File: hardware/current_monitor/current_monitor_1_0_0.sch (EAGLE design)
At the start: 60 parts, among them Q1 RZQ045P01CT, Q2 APDS-9002, U1 PIC18F46J50, U4 MAX4372, U5 TC1046, U6 AT45DB041BWIDE, U7 AT45DB041BWIDE, X1 USBSMD

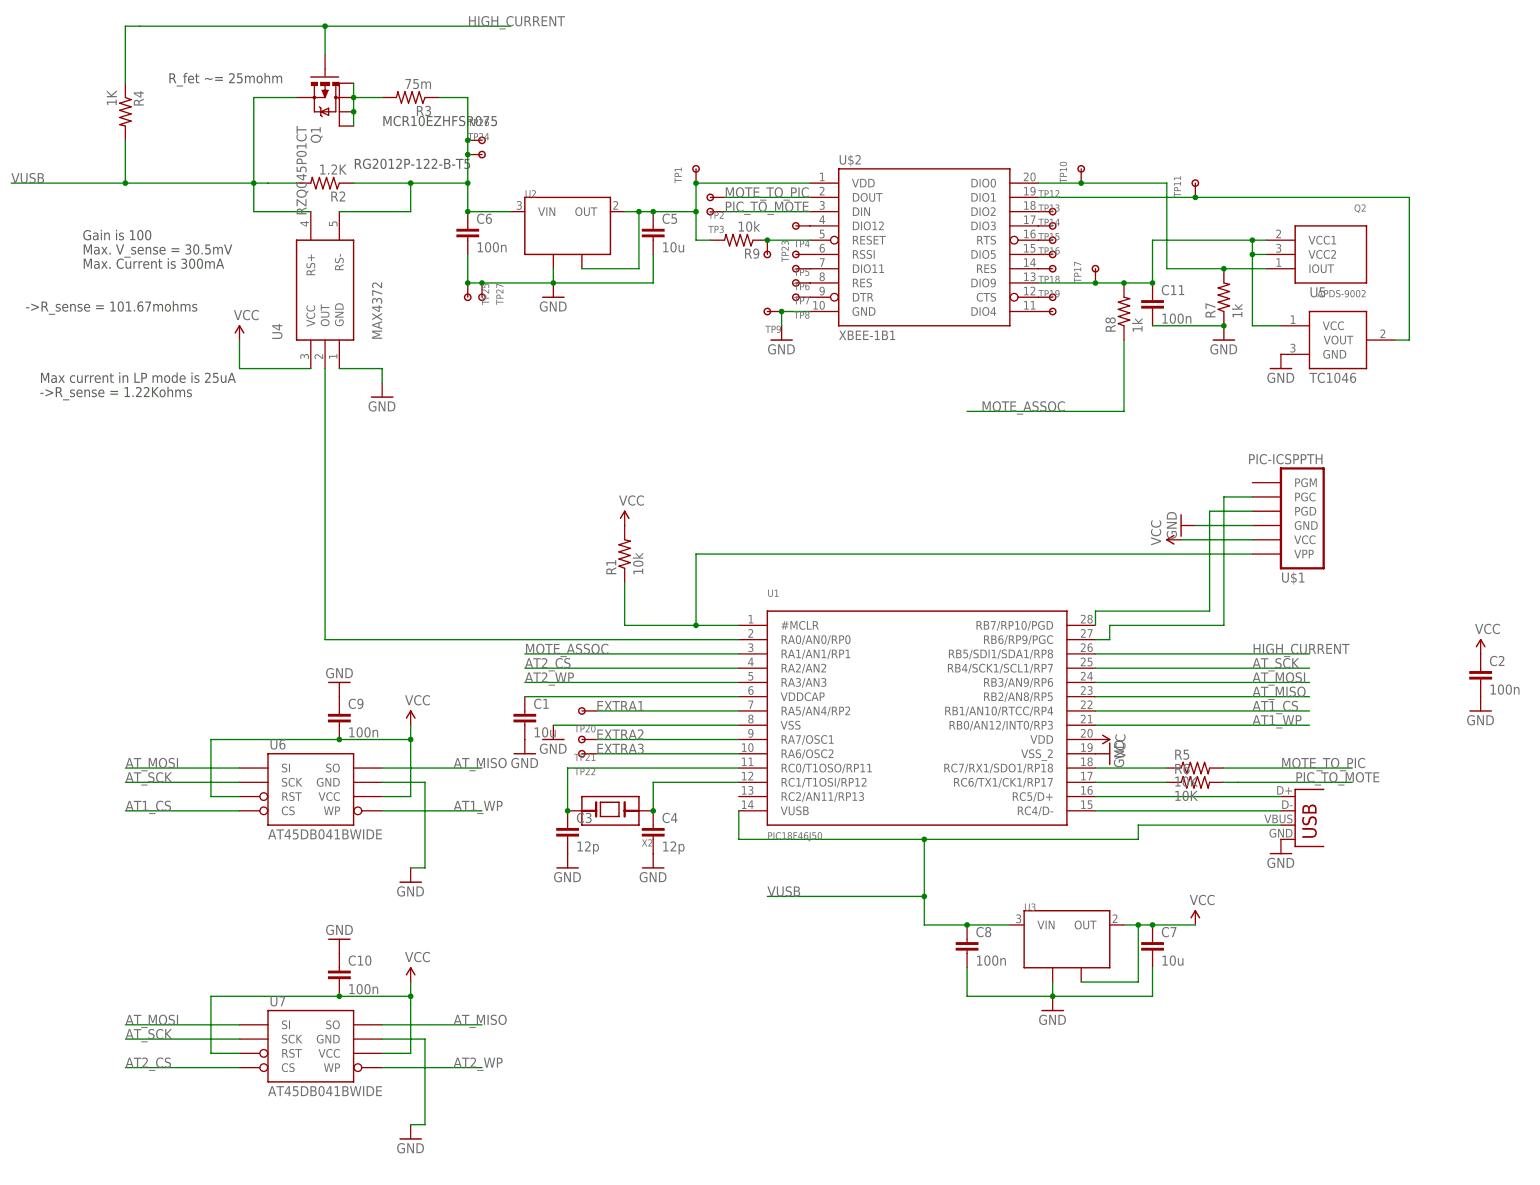
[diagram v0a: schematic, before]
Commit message: current monitoring board changes
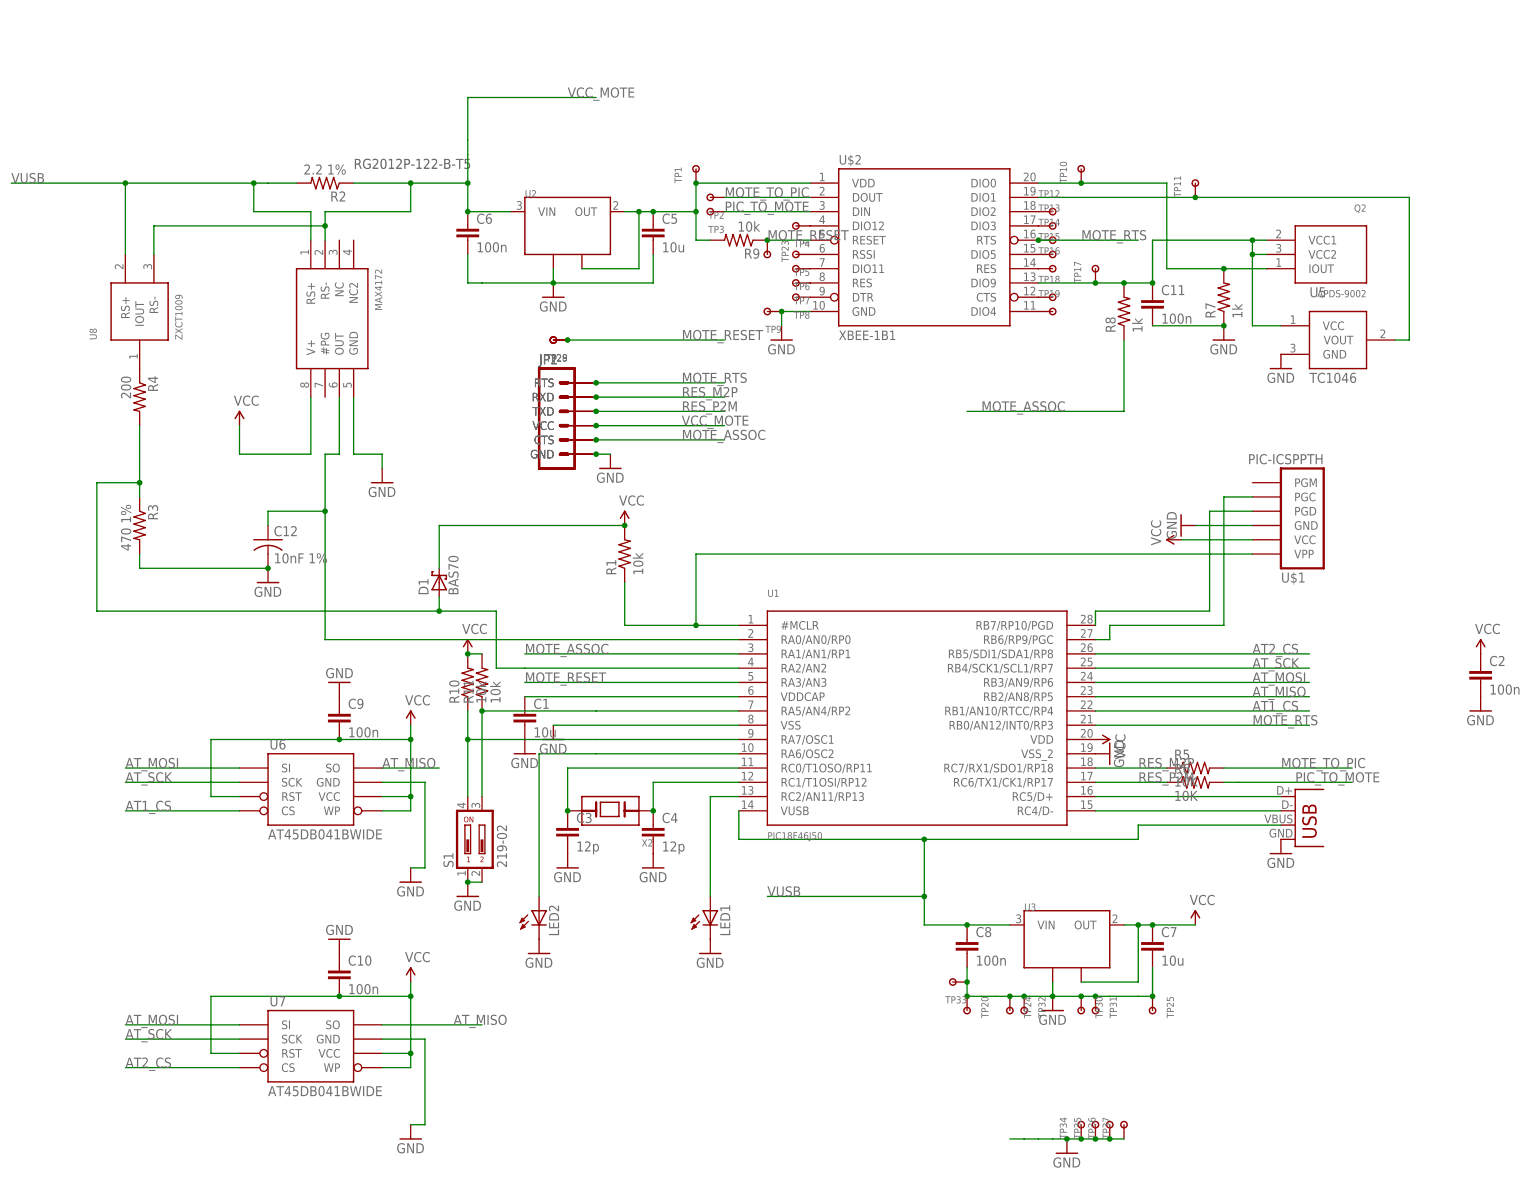
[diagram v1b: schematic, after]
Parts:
- removed Q1: RZQ045P01CT, WSNlib:MOSFET-PCHANNEL-D4
- removed TP21, TP22, TP26, TP27: TESTPOINT100MIL, WSNlib:TESTPOINT100MIL
- added C12: 10nF 1%, rcl:C-USC1812
- added D1: BAS70, diode:BAS70
- added JP1, JP2: (no value), custom:FTDI_CABLESIP
- added LED1, LED2: (no value), led:LEDCHIP-LED0805
- added R10, R11: 10k, SparkFun:RESISTOR
- added S1: 219-02, switch-dil:219-02
- added TP28, TP29: TESTPOINT100MIL, WSNlib:TESTPOINT100MIL
- added TP30, TP31, TP32, TP33: TESTPOINTSMALLEST, WSNlib:TESTPOINTSMALLEST
- added TP34, TP35, TP36, TP37: TESTPOINTM3, WSNlib:TESTPOINTM3
- added U8: ZXCT1009, WSNlib:ZXCT1009
- R2: value 1.2K -> 2.2 1%
- R3: value 75m -> 470 1%
- R4: value 1K -> 200
- TP20, TP24, TP25: value TESTPOINT100MIL -> TESTPOINTSMALLEST; device WSNlib:TESTPOINT100MIL -> WSNlib:TESTPOINTSMALLEST
- U4: value MAX4372 -> MAX4172; device WSNlib:MAX4372 -> WSNlib:MAX4172
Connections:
- removed net AT1_WP: U1.RB0/AN12/INT0/RP3, U6.WP
- removed net AT2_WP: U1.RA3/AN3, U7.WP
- removed net HIGH_CURRENT: Q1.G, R4.1, U1.RB5/SDI1/SDA1/RP8
- removed net N$14: R6.1, U1.RC6/TX1/CK1/RP17
- removed net N$20: R9.1, TP23.P$1, U$2.RESET
- removed net N$29: TP14.P$1, U$2.RTS
- new net MOTE_RESET: R9.1, TP23.P$1, TP28.P$1, TP29.P$1, U$2.RESET, U1.RA3/AN3
- new net MOTE_RTS: JP1.RTS, JP2.RTS, TP14.P$1, U$2.RTS, U1.RB0/AN12/INT0/RP3
- new net RES_M2P: JP1.RXD, JP2.RXD, R5.1, U1.RC7/RX1/SDO1/RP18
- new net RES_P2M: JP1.TXD, JP2.TXD, R6.1, U1.RC6/TX1/CK1/RP17
- new net VCC_MOTE: C6.1, JP1.VCC, JP2.VCC, R2.1, U2.VIN, U4.RS-, U8.RS-
- net AT2_CS: now also U1.RB5/SDI1/SDA1/RP8; no longer U1.RA2/AN2
- net EXTRA1: now also R11.1, S1.3; no longer TP20.P$1
- net EXTRA2: now also R10.1, S1.4; no longer TP21.P$1
- net EXTRA3: now also LED2.A; no longer TP22.P$1
- net GND: now also C12.2, JP1.GND, JP2.GND, LED1.C, LED2.C, R3.2, S1.1, S1.2, TP20.P$1, TP24.P$1, TP30.P$1, TP31.P$1, TP32.P$1, TP33.P$1, TP34.P$1, TP35.P$1, TP36.P$1, TP37.P$1; no longer TP27.P$1
- net MOTE_ASSOC: now also JP1.CTS, JP2.CTS
- net N$11: now also C12.1
- net N$12: now also D1.A, R3.1, R4.2, U1.RA2/AN2; no longer Q1.D, Q1.D1, Q1.D2, Q1.D3, R3.2
- net N$13: now also R4.1, U8.IOUT; no longer R5.1, U1.RC7/RX1/SDO1/RP18
- net N$3: now also LED1.A, U1.RC2/AN11/RP13; no longer C6.1, R2.1, R3.1, TP24.P$1, TP26.P$1, U2.VIN, U4.RS-
- net VCC: now also D1.C, R10.2, R11.2, U4.V+, U6.WP, U7.WP; no longer U4.VCC
- net VUSB: now also U8.RS+; no longer Q1.S, R4.2
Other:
- note removed: "->R_sense = 1.22Kohms"
- note removed: "->R_sense = 101.67mohms"
- note removed: "Gain is 100"
- note removed: "MCR10EZHFSR075"
- note removed: "Max current in LP mode is 25uA"
- note removed: "Max. Current is 300mA"
- note removed: "Max. V_sense = 30.5mV"
- note removed: "R_fet ~= 25mohm"
- moved on the sheet: R3, R4, TP20, TP24, TP25

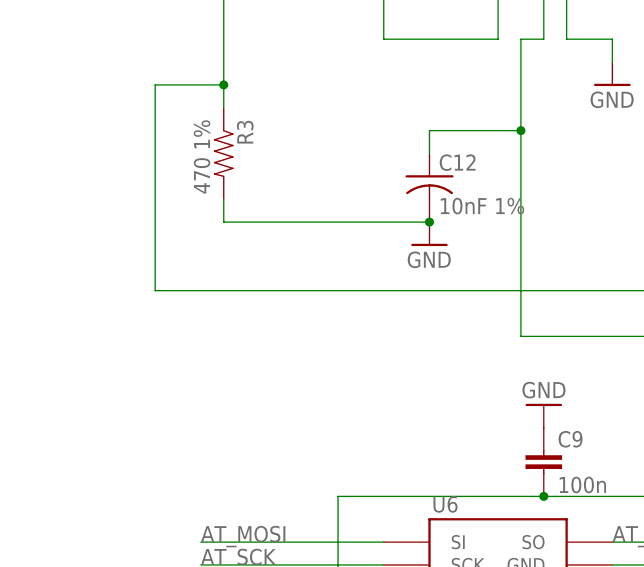
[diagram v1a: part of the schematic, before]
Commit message: Changes/additions of files related to current monitoring
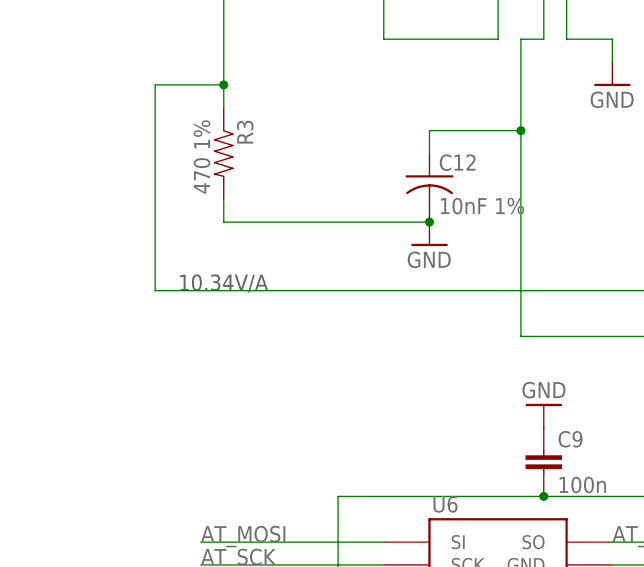
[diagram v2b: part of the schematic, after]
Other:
- note added: "10.34V/A"
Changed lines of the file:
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@@
 <plain>
 <text x="-35.56" y="152.4" size="1.778" layer="97">RG2012P-122-B-T5</text>
+<text x="-78.74" y="73.66" size="1.778" layer="97">10.34V/A</text>
 </plain>
 <instances>
